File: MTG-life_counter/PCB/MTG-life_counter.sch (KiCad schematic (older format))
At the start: 37 parts, among them J2 AVR-ISP-6, Q1 IRLML6244, Q2 Si2301DS, Q3 Si2301DS, U2 AT90S4433-8P, U3 HDSP-H101, U4 HDSP-H101, Y1 8 MHz

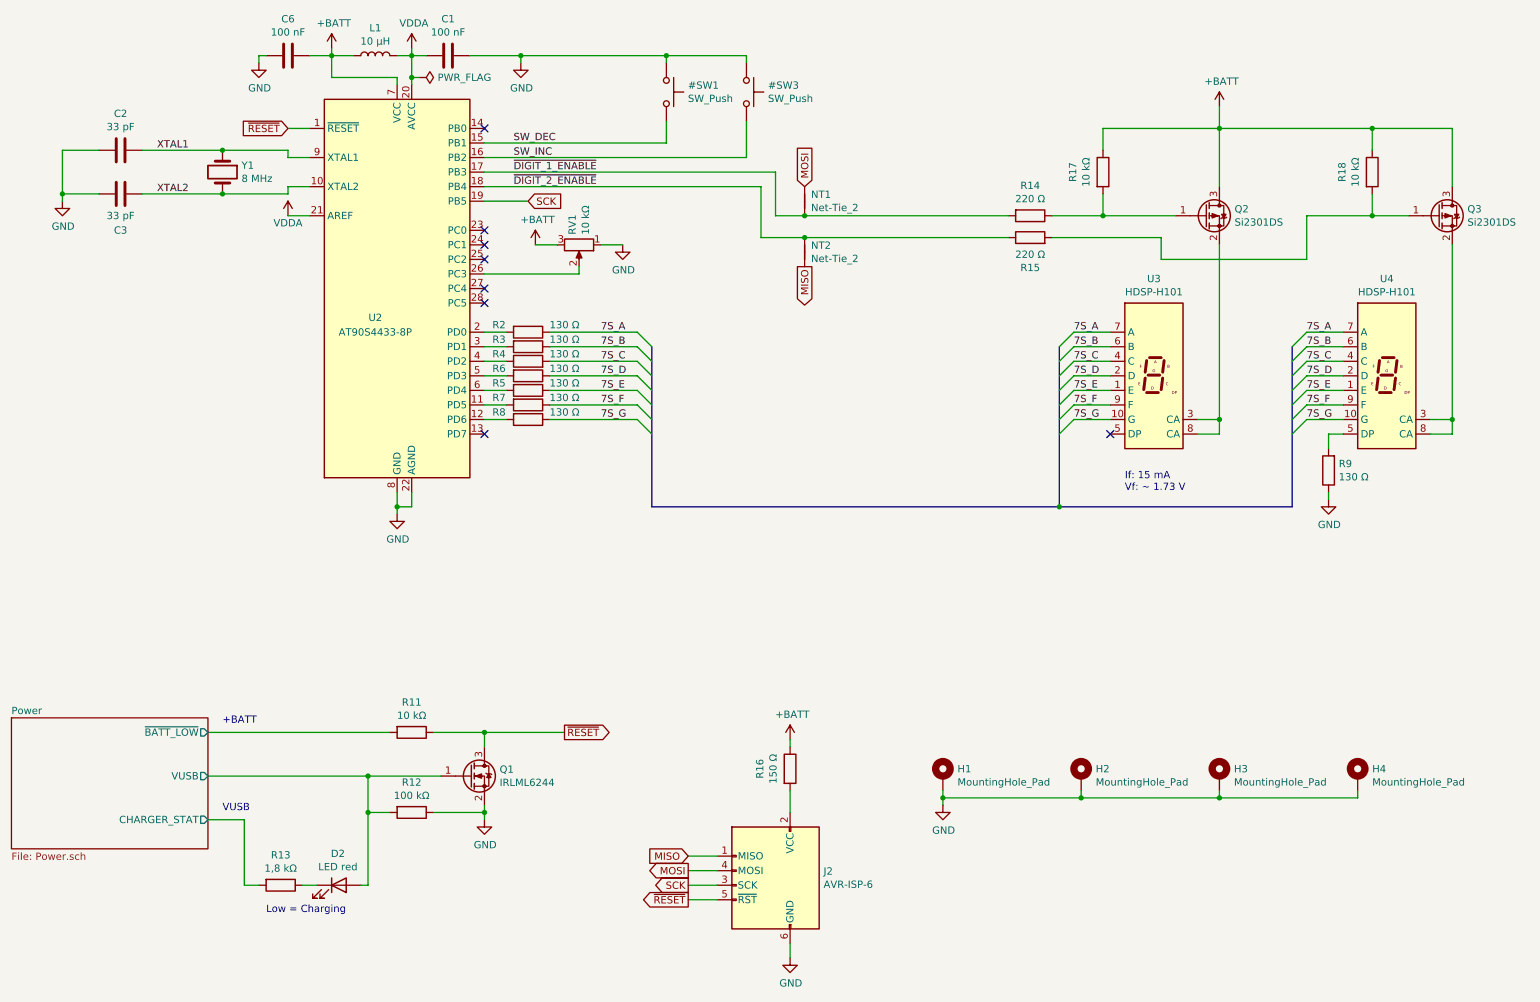
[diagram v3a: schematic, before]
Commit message: The placing & routing is pretty much done, except GND.
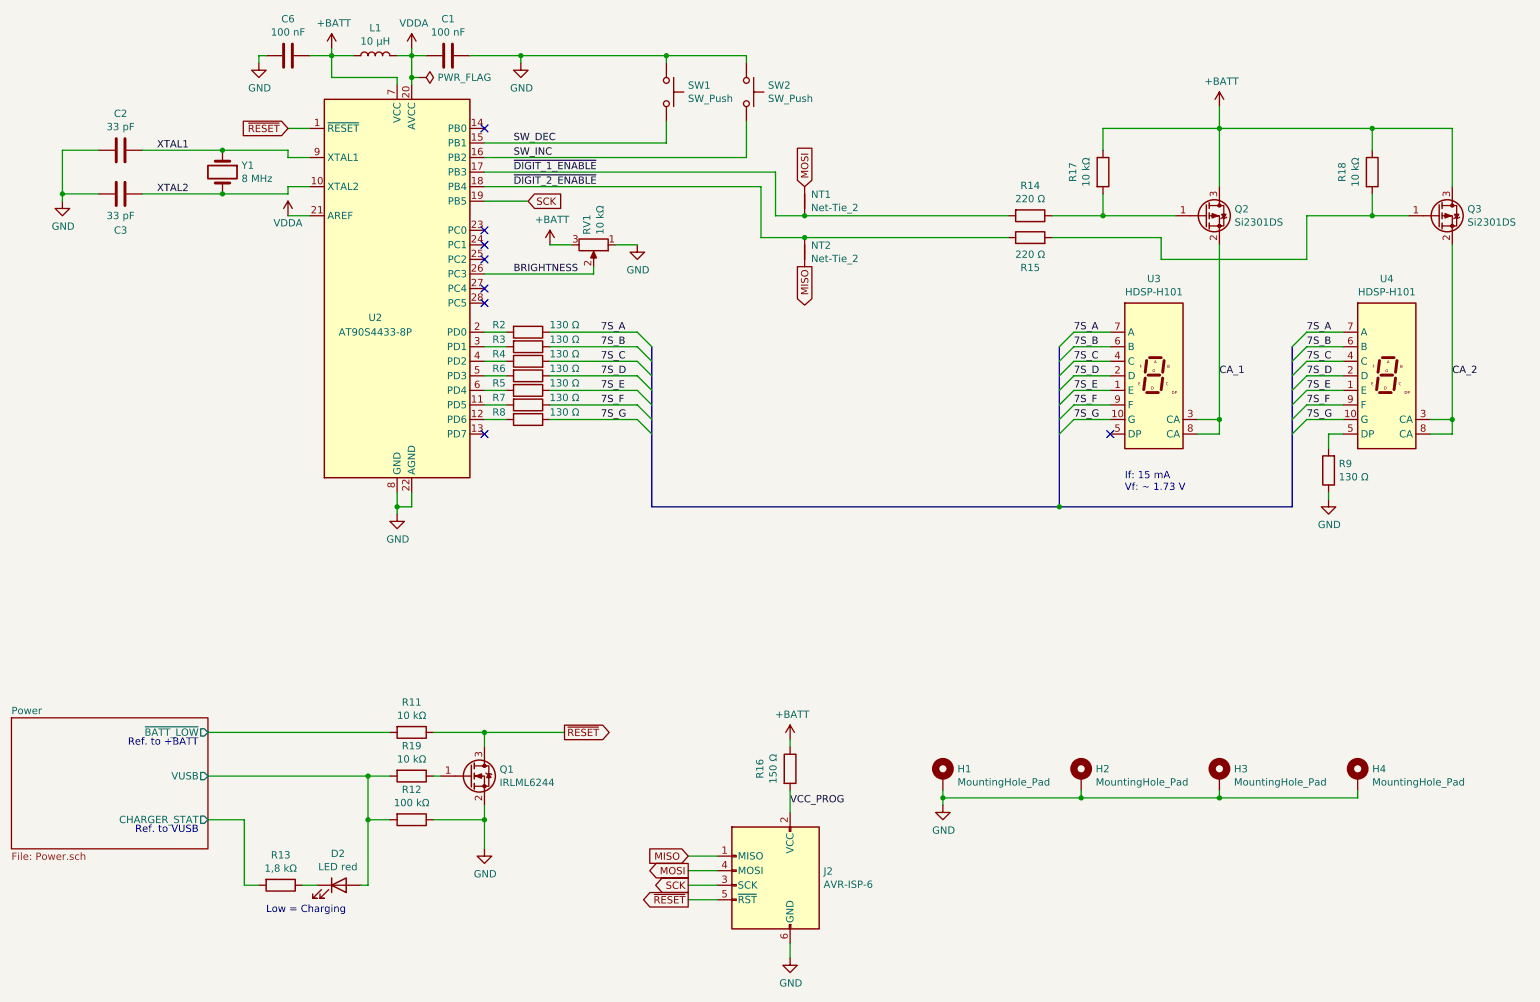
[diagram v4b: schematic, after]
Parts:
- added R19: 10 kΩ, Resistor_SMD:R_0805_2012Metric_Pad1.20x1.40mm_HandSolder, symbol Device:R
- added SW1, SW2: SW_Push, Connector_Wire:SolderWire-0.15sqmm_1x02_P4mm_D0.5mm_OD1.5mm, symbol Switch:SW_Push
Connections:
- net GND: now also SW1.1, SW2.1
- net Power/VUSB: now also R19.2; no longer Q1.1 (G)
- net SW_DEC: now also SW1.2
- net SW_INC: now also SW2.2
- net BRIGHTNESS: now reaches RV1.2, U2.26 (PC3)
- net CA_1: now reaches Q2.2 (S), U3.3 (CA), U3.8 (CA)
- net CA_2: now reaches Q3.2 (S), U4.3 (CA), U4.8 (CA)
- net VCC_PROG: now reaches J2.2 (VCC), R16.2
- new net: Q1.1 (G), R19.1
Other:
- note added: "Ref. to +BATT"
- note added: "Ref. to VUSB"
- note removed: "+BATT"
- note removed: "VUSB"
- moved on the sheet: R12, RV1
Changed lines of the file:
@@
 	2750 2050 2900 2050
 $Comp
-L Switch:SW_Push #SW3
+L Switch:SW_Push SW2
 U 1 1 6144BFDF
 P 5900 1400
-F 0 "#SW3" V 5854 1548 50  0000 L CNN
+F 0 "SW2" V 5854 1548 50  0000 L CNN
 F 1 "SW_Push" V 5945 1548 50  0000 L CNN
-F 2 "" H 5900 1600 50  0001 C CNN
+F 2 "Connector_Wire:SolderWire-0.15sqmm_1x02_P4mm_D0.5mm_OD1.5mm" H 5900 1600 50  0001 C CNN
 F 3 "~" H 5900 1600 50  0001 C CNN
 	1    5900 1400
-	0    1    1    0
-$EndComp
-$Comp
-L Switch:SW_Push #SW1
-U 1 1 6144D59E
-P 5350 1400
-F 0 "#SW1" V 5304 1548 50  0000 L CNN
-F 1 "SW_Push" V 5395 1548 50  0000 L CNN
-F 2 "" H 5350 1600 50  0001 C CNN
-F 3 "~" H 5350 1600 50  0001 C CNN
-	1    5350 1400
 	0    1    1    0
 $EndComp
@@
 L power:GND #PWR012
 U 1 1 619FDBF8
-P 4100 6400
-F 0 "#PWR012" H 4100 6150 50  0001 C CNN
-F 1 "GND" H 4105 6227 50  0000 C CNN
-F 2 "" H 4100 6400 50  0001 C CNN
-F 3 "" H 4100 6400 50  0001 C CNN
-	1    4100 6400
-	1    0    0    -1
-$EndComp
-Wire Wire Line
-	4100 6400 4100 6350
+P 4100 6600
+F 0 "#PWR012" H 4100 6350 50  0001 C CNN
+F 1 "GND" H 4105 6427 50  0000 C CNN
+F 2 "" H 4100 6600 50  0001 C CNN
+F 3 "" H 4100 6600 50  0001 C CNN
+	1    4100 6600
+	1    0    0    -1
+$EndComp
+Wire Wire Line
+	4100 6600 4100 6400
 Text GLabel 4650 5800 2    50   Output ~ 0
 ~RESET
@@
 L Device:R R12
 U 1 1 61A098B5
-P 3600 6350
-F 0 "R12" V 3393 6350 50  0000 C CNN
-F 1 "100 kΩ" V 3484 6350 50  0000 C CNN
-F 2 "Resistor_SMD:R_0805_2012Metric_Pad1.20x1.40mm_HandSolder" V 3530 6350 50  0001 C CNN
-F 3 "~" H 3600 6350 50  0001 C CNN
-	1    3600 6350
-	0    1    1    0
-$EndComp
-Wire Wire Line
-	3450 6350 3300 6350
-Wire Wire Line
-	3300 6350 3300 6100
+P 3600 6400
+F 0 "R12" V 3393 6400 50  0000 C CNN
+F 1 "100 kΩ" V 3484 6400 50  0000 C CNN
+F 2 "Resistor_SMD:R_0805_2012Metric_Pad1.20x1.40mm_HandSolder" V 3530 6400 50  0001 C CNN
+F 3 "~" H 3600 6400 50  0001 C CNN
+	1    3600 6400
+	0    1    1    0
+$EndComp
+Wire Wire Line
+	3450 6400 3300 6400
+Wire Wire Line
+	3300 6400 3300 6100
 Connection ~ 3300 6100
 Wire Wire Line
-	3300 6100 3800 6100
-Wire Wire Line
-	3750 6350 4100 6350
-Connection ~ 4100 6350
-Wire Wire Line
-	4100 6350 4100 6300
+	3300 6100 3450 6100
+Wire Wire Line
+	3750 6400 4100 6400
+Connection ~ 4100 6400
+Wire Wire Line
+	4100 6400 4100 6300
 Wire Wire Line
 	2200 5800 3450 5800
@@
 	1    0    0    -1
 $EndComp
-Text Notes 2300 5750 0    50   ~ 0
-+BATT
+Text Notes 1650 5900 0    50   ~ 0
+Ref. to +BATT
 $Comp
 L Device:LED D2
@@
 	3250 6850 3300 6850
 Wire Wire Line
-	3300 6850 3300 6350
-Connection ~ 3300 6350
+	3300 6850 3300 6400
+Connection ~ 3300 6400
 Wire Wire Line
 	2950 6850 2850 6850
@@
 Wire Wire Line
 	2450 6400 2200 6400
-Text Notes 2300 6350 0    50   ~ 0
-VUSB
+Text Notes 1700 6500 0    50   ~ 0
+Ref. to VUSB
 Text Notes 2600 7050 0    50   ~ 0
 Low = Charging
@@
 L Device:R_POT RV1
 U 1 1 61456388
-P 4750 2450
-F 0 "RV1" H 4680 2404 50  0000 R CNN
-F 1 "10 kΩ" H 4680 2495 50  0000 R CNN
-F 2 "Potentiometer_THT:Potentiometer_Piher_PT-10-H01_Horizontal" H 4750 2450 50  0001 C CNN
-F 3 "~" H 4750 2450 50  0001 C CNN
-	1    4750 2450
+P 4850 2450
+F 0 "RV1" H 4780 2404 50  0000 R CNN
+F 1 "10 kΩ" H 4780 2495 50  0000 R CNN
+F 2 "Potentiometer_THT:Potentiometer_Piher_PT-10-H01_Horizontal" H 4850 2450 50  0001 C CNN
+F 3 "~" H 4850 2450 50  0001 C CNN
+	1    4850 2450
 	0    1    1    0
 $EndComp
@@
 L power:+BATT #PWR0102
 U 1 1 61C17C07
-P 4450 2450
-F 0 "#PWR0102" H 4450 2300 50  0001 C CNN
-F 1 "+BATT" H 4465 2623 50  0000 C CNN
-F 2 "" H 4450 2450 50  0001 C CNN
-F 3 "" H 4450 2450 50  0001 C CNN
-	1    4450 2450
+P 4550 2450
+F 0 "#PWR0102" H 4550 2300 50  0001 C CNN
+F 1 "+BATT" H 4565 2623 50  0000 C CNN
+F 2 "" H 4550 2450 50  0001 C CNN
+F 3 "" H 4550 2450 50  0001 C CNN
+	1    4550 2450
 	1    0    0    -1
 $EndComp
@@
 L power:GND #PWR011
 U 1 1 6146287A
-P 5050 2450
-F 0 "#PWR011" H 5050 2200 50  0001 C CNN
-F 1 "GND" H 5055 2277 50  0000 C CNN
-F 2 "" H 5050 2450 50  0001 C CNN
-F 3 "" H 5050 2450 50  0001 C CNN
-	1    5050 2450
-	1    0    0    -1
-$EndComp
-Wire Wire Line
-	4900 2450 5050 2450
-Wire Wire Line
-	4450 2450 4600 2450
-Wire Wire Line
-	4750 2650 4750 2600
-Wire Wire Line
-	4100 2650 4750 2650
+P 5150 2450
+F 0 "#PWR011" H 5150 2200 50  0001 C CNN
+F 1 "GND" H 5155 2277 50  0000 C CNN
+F 2 "" H 5150 2450 50  0001 C CNN
+F 3 "" H 5150 2450 50  0001 C CNN
+	1    5150 2450
+	1    0    0    -1
+$EndComp
+Wire Wire Line
+	5000 2450 5150 2450
+Wire Wire Line
+	4550 2450 4700 2450
+Wire Wire Line
+	4850 2650 4850 2600
+Wire Wire Line
+	4100 2650 4850 2650
 Wire Wire Line
 	6000 2050 6000 2400
@@
 Wire Wire Line
 	1750 1800 2300 1800
+Connection ~ 2300 1800
+Text Label 4300 2650 0    50   ~ 0
+BRIGHTNESS
+$Comp
+L Device:R R19
+U 1 1 62CE8F9E
+P 3600 6100
+F 0 "R19" V 3393 6100 50  0000 C CNN
+F 1 "10 kΩ" V 3484 6100 50  0000 C CNN
+F 2 "Resistor_SMD:R_0805_2012Metric_Pad1.20x1.40mm_HandSolder" V 3530 6100 50  0001 C CNN
+F 3 "~" H 3600 6100 50  0001 C CNN
+	1    3600 6100
+	0    1    1    0
+$EndComp
+Wire Wire Line
+	3750 6100 3800 6100
+Text Label 9150 3350 0    50   ~ 0
+CA_1
+Text Label 10750 3350 0    50   ~ 0
+CA_2
+$Comp
+L Switch:SW_Push SW1
+U 1 1 6144D59E
+P 5350 1400
+F 0 "SW1" V 5304 1548 50  0000 L CNN
+F 1 "SW_Push" V 5395 1548 50  0000 L CNN
+F 2 "Connector_Wire:SolderWire-0.15sqmm_1x02_P4mm_D0.5mm_OD1.5mm" H 5350 1600 50  0001 C CNN
+F 3 "~" H 5350 1600 50  0001 C CNN
+	1    5350 1400
+	0    1    1    0
+$EndComp
 Wire Bus Line
 	5250 3150 5250 4250
@@
 Wire Bus Line
 	9650 3150 9650 4250
-Connection ~ 2300 1800
+Text Label 6200 6300 0    50   ~ 0
+VCC_PROG
 $EndSCHEMATC

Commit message: Correct footprint for the NetTies.
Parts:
- NT1, NT2: footprint NetTie:NetTie-2_SMD_Pad0.5mm -> mibe:NetTie-2_SMD_Pad0.25mm
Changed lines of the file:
@@
 F 0 "NT2" V 6254 2544 50  0000 L CNN
 F 1 "Net-Tie_2" V 6345 2544 50  0000 L CNN
-F 2 "NetTie:NetTie-2_SMD_Pad0.5mm" H 6300 2500 50  0001 C CNN
+F 2 "mibe:NetTie-2_SMD_Pad0.25mm" H 6300 2500 50  0001 C CNN
 F 3 "~" H 6300 2500 50  0001 C CNN
 	1    6300 2500
@@
 F 0 "NT1" V 6254 2194 50  0000 L CNN
 F 1 "Net-Tie_2" V 6345 2194 50  0000 L CNN
-F 2 "NetTie:NetTie-2_SMD_Pad0.5mm" H 6300 2150 50  0001 C CNN
+F 2 "mibe:NetTie-2_SMD_Pad0.25mm" H 6300 2150 50  0001 C CNN
 F 3 "~" H 6300 2150 50  0001 C CNN
 	1    6300 2150
@@
 	0    1    1    0
 $EndComp
+Text Label 6200 6300 0    50   ~ 0
+VCC_PROG
 Wire Bus Line
 	5250 3150 5250 4250
@@
 Wire Bus Line
 	9650 3150 9650 4250
-Text Label 6200 6300 0    50   ~ 0
-VCC_PROG
 $EndSCHEMATC

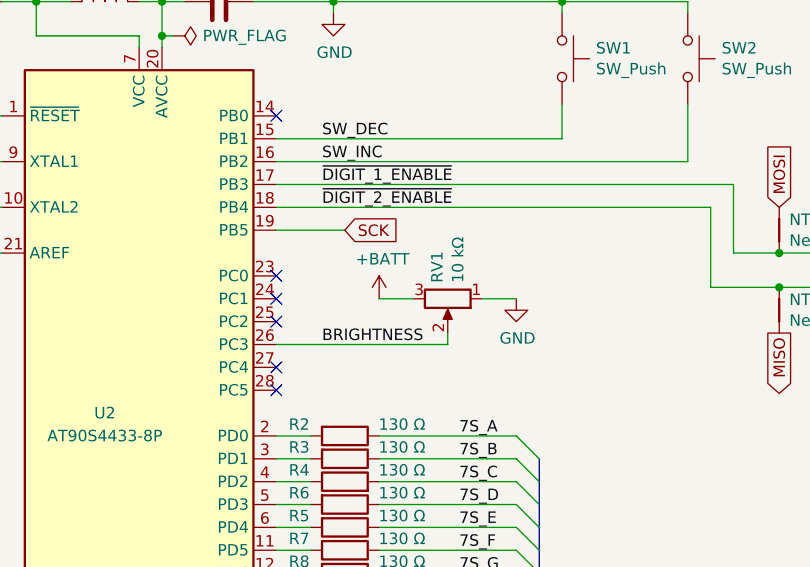
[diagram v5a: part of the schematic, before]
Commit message: Removed brightness feature.
This closes #11.
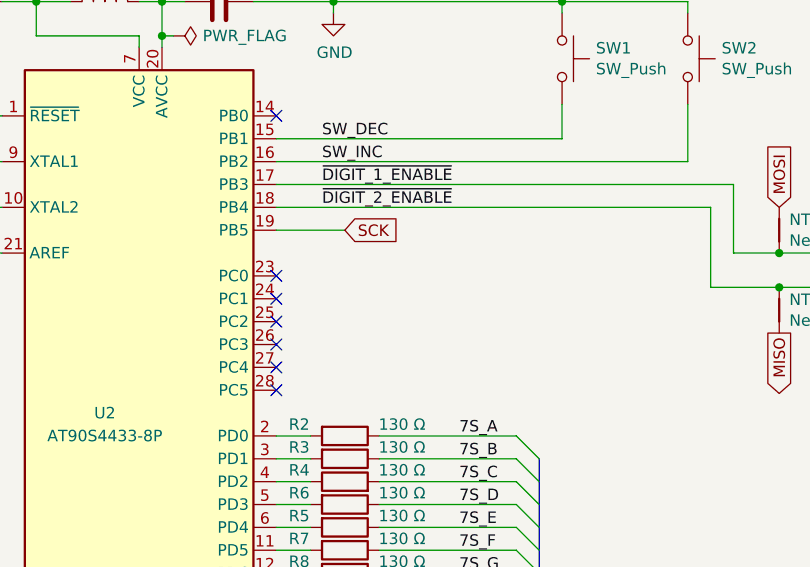
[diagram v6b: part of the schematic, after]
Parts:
- removed RV1: 10 kΩ, Potentiometer_THT:Potentiometer_Piher_PT-10-H01_Horizontal, symbol Device:R_POT
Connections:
- net BRIGHTNESS: no longer names the net of U2.26 (PC3)
- no-connect marks 8 -> 9
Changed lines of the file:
@@
 Text Label 4300 2050 0    50   ~ 0
 ~DIGIT_2_ENABLE
-$Comp
-L Device:R_POT RV1
-U 1 1 61456388
-P 4850 2450
-F 0 "RV1" H 4780 2404 50  0000 R CNN
-F 1 "10 kΩ" H 4780 2495 50  0000 R CNN
-F 2 "Potentiometer_THT:Potentiometer_Piher_PT-10-H01_Horizontal" H 4850 2450 50  0001 C CNN
-F 3 "~" H 4850 2450 50  0001 C CNN
-	1    4850 2450
-	0    1    1    0
-$EndComp
 Wire Wire Line
 	8000 2400 8750 2400
 Wire Wire Line
 	8750 2400 8750 2550
-$Comp
-L power:+BATT #PWR0102
-U 1 1 61C17C07
-P 4550 2450
-F 0 "#PWR0102" H 4550 2300 50  0001 C CNN
-F 1 "+BATT" H 4565 2623 50  0000 C CNN
-F 2 "" H 4550 2450 50  0001 C CNN
-F 3 "" H 4550 2450 50  0001 C CNN
-	1    4550 2450
-	1    0    0    -1
-$EndComp
-$Comp
-L power:GND #PWR011
-U 1 1 6146287A
-P 5150 2450
-F 0 "#PWR011" H 5150 2200 50  0001 C CNN
-F 1 "GND" H 5155 2277 50  0000 C CNN
-F 2 "" H 5150 2450 50  0001 C CNN
-F 3 "" H 5150 2450 50  0001 C CNN
-	1    5150 2450
-	1    0    0    -1
-$EndComp
-Wire Wire Line
-	5000 2450 5150 2450
-Wire Wire Line
-	4550 2450 4700 2450
-Wire Wire Line
-	4850 2650 4850 2600
-Wire Wire Line
-	4100 2650 4850 2650
 Wire Wire Line
 	6000 2050 6000 2400
@@
 	1750 1800 2300 1800
 Connection ~ 2300 1800
-Text Label 4300 2650 0    50   ~ 0
-BRIGHTNESS
 $Comp
 L Device:R R19
@@
 Text Label 6200 6300 0    50   ~ 0
 VCC_PROG
+NoConn ~ 4100 2650
 Wire Bus Line
 	5250 3150 5250 4250

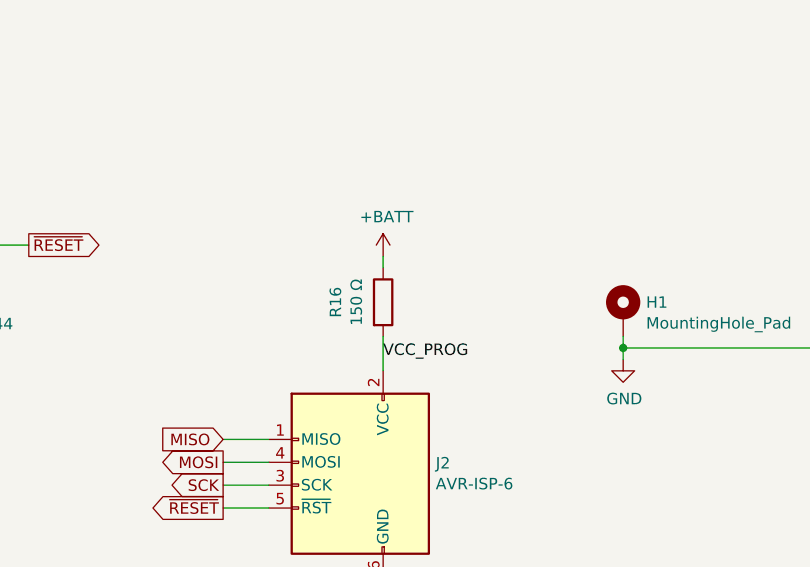
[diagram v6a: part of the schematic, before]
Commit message: Remove R16 to fix #8.
The chances of the battery and programmer connected at the same time is there but actually pretty low. To flash the micro-controller you would disconnect the battery because of the easier handling alone...
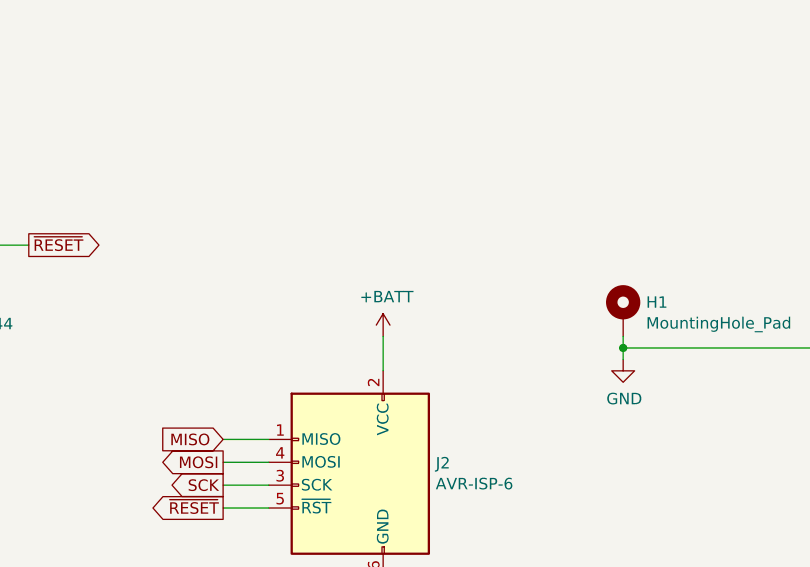
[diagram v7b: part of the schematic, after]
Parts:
- removed R16: 150 Ω, Resistor_SMD:R_0805_2012Metric_Pad1.20x1.40mm_HandSolder, symbol Device:R
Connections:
- net VCC_PROG is gone; now on net +BATT: J2.2 (VCC)
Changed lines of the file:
@@
-$EndComp
-$Comp
-L Device:R R16
-U 1 1 61C193F0
-P 6200 6050
-F 0 "R16" V 5993 6050 50  0000 C CNN
-F 1 "150 Ω" V 6084 6050 50  0000 C CNN
-F 2 "Resistor_SMD:R_0805_2012Metric_Pad1.20x1.40mm_HandSolder" V 6130 6050 50  0001 C CNN
-F 3 "~" H 6200 6050 50  0001 C CNN
-	1    6200 6050
-	1    0    0    -1
 $EndComp
 $Comp
 L power:+BATT #PWR05
 U 1 1 61C19A2C
-P 6200 5850
-F 0 "#PWR05" H 6200 5700 50  0001 C CNN
-F 1 "+BATT" H 6215 6023 50  0000 C CNN
-F 2 "" H 6200 5850 50  0001 C CNN
-F 3 "" H 6200 5850 50  0001 C CNN
-	1    6200 5850
+P 6200 6200
+F 0 "#PWR05" H 6200 6050 50  0001 C CNN
+F 1 "+BATT" H 6215 6373 50  0000 C CNN
+F 2 "" H 6200 6200 50  0001 C CNN
+F 3 "" H 6200 6200 50  0001 C CNN
+	1    6200 6200
 	1    0    0    -1
 $EndComp
-Wire Wire Line
-	6200 5850 6200 5900
-Wire Wire Line
-	6200 6200 6200 6350
 $Comp
 L Device:R R14
@@
 	0    1    1    0
 $EndComp
-Text Label 6200 6300 0    50   ~ 0
-VCC_PROG
 NoConn ~ 4100 2650
+Wire Wire Line
+	6200 6200 6200 6350
 Wire Bus Line
 	5250 3150 5250 4250
